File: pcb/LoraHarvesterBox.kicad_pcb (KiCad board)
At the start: 4 copper layers, 48 x 45.5 mm, 42 parts, among them J1 Conn_01x02_Pin, J2 Conn_01x02_Pin, J3 Conn_01x02_Pin, J4 Conn_01x04_Socket, J5 Conn_01x04_Socket, J6 Conn_01x04_Socket, J7 Conn_01x04_Socket, J8 Conn_01x06_Socket, SW1 SSSS811101, SW2 TS-1088-AR02016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

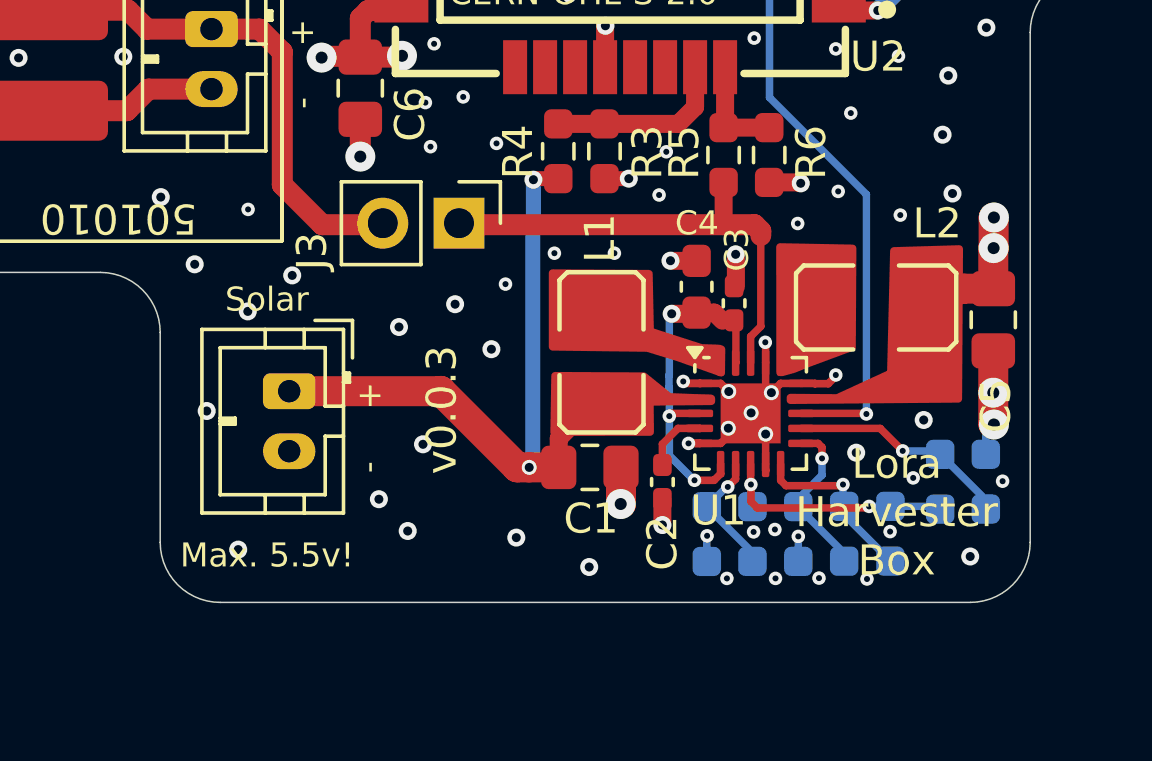
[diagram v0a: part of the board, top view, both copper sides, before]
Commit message: pcb: move silk screens and jumper around
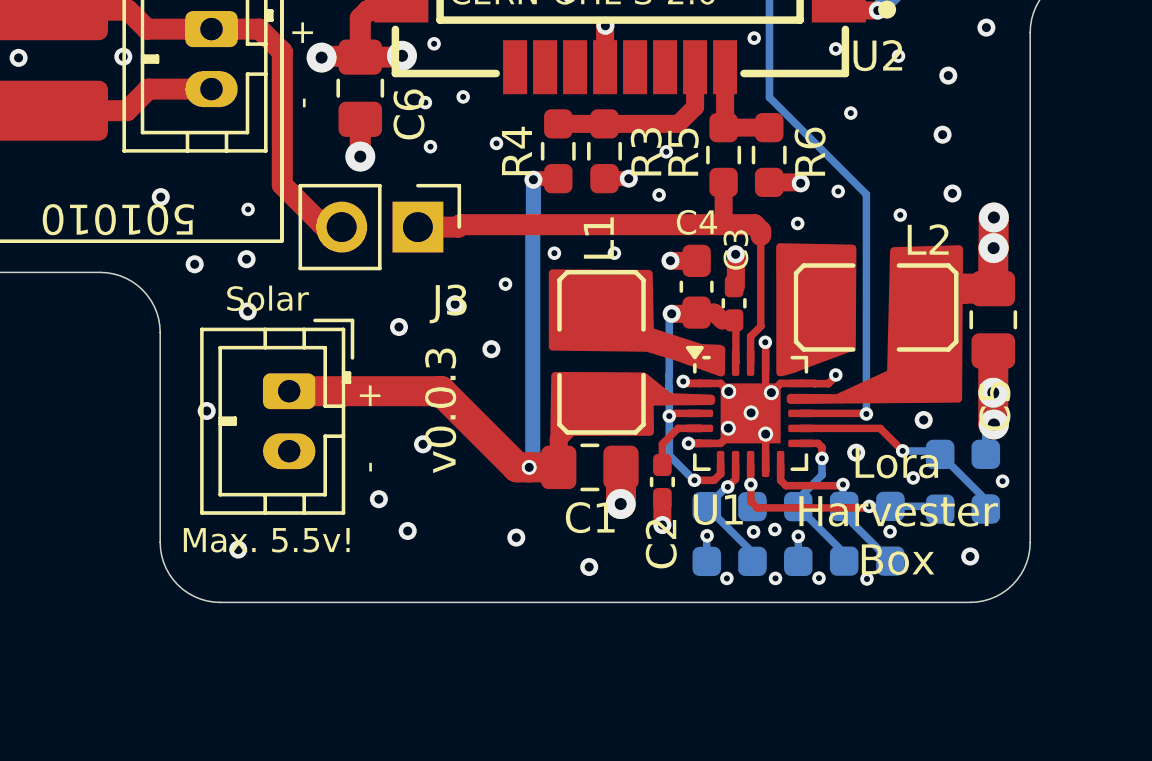
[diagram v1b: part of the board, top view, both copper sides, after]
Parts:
- moved J3 1.38 mm to (118.6, 87.5)
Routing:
- net /VBAT: track 16.1 -> 17.5 mm
- net Net-(BT1-+): track 17.7 -> 16.4 mm
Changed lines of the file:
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@@
 	(footprint "Connector_PinHeader_2.54mm:PinHeader_1x02_P2.54mm_Vertical"
 		(layer "F.Cu")
-		(at 119.96 87.36 -90)
+		(at 118.59 87.49 -90)
 		(descr "Through hole straight pin header, 1x02, 2.54mm pitch, single row")
 		(tags "Through hole pin header THT 1x02 2.54mm single row")
 		(property "Reference" "J3"
-			(at 0.93 4.9 90)
+			(at 2.47 -1.1 0)
 			(layer "F.SilkS")
 			(effects
@@
 		(at 133.86375 90.17)
 		(property "Reference" "L2"
-			(at 2.03625 -2.8 0)
+			(at 1.73625 -2.22 0)
 			(layer "F.SilkS")
 			(effects
@@
 	)
 	(gr_text "Max. 5.5v!"
-		(at 110.66 98.9 0)
+		(at 110.68 98.42 0)
 		(layer "F.SilkS")
 		(effects
@@
 	)
 	(segment
+		(start 128.76 87.41)
+		(end 120.01 87.41)
+		(width 0.7)
+		(layer "F.Cu")
+		(net 1)
+	)
+	(segment
 		(start 128.78 87.39)
 		(end 128.76 87.41)
@@
 	)
 	(segment
-		(start 128.76 87.41)
-		(end 120.01 87.41)
-		(width 0.7)
-		(layer "F.Cu")
-		(net 1)
-	)
-	(segment
 		(start 120.01 87.41)
-		(end 119.96 87.36)
+		(end 119.93 87.49)
 		(width 0.7)
 		(layer "F.Cu")
@@
 	)
 	(segment
+		(start 119.93 87.49)
+		(end 118.59 87.49)
+		(width 0.7)
+		(layer "F.Cu")
+		(net 1)
+	)
+	(segment
 		(start 129.81 87.41)
 		(end 128.76 87.41)
@@
 	)
 	(via
-		(at 114.4 89.1)
+		(at 112.88 88.56)
 		(size 0.6)
 		(drill 0.3)
@@
 	)
 	(segment
-		(start 113.31 80.89)
-		(end 111.71 80.89)
+		(start 115.97 87.41)
+		(end 115.4 87.41)
 		(width 0.7)
 		(layer "F.Cu")
@@
 	)
 	(segment
-		(start 109.56 80.89)
-		(end 111.71 80.89)
+		(start 116.05 87.49)
+		(end 115.97 87.41)
 		(width 0.7)
 		(layer "F.Cu")
@@
 	)
 	(segment
-		(start 114.07 81.65)
-		(end 113.31 80.89)
+		(start 115.4 87.41)
+		(end 114.07 86.08)
 		(width 0.7)
 		(layer "F.Cu")
@@
 	)
 	(segment
-		(start 117.42 87.36)
-		(end 117.37 87.41)
+		(start 109.56 80.89)
+		(end 111.71 80.89)
 		(width 0.7)
 		(layer "F.Cu")
@@
 	)
 	(segment
-		(start 108.93 80.26)
-		(end 109.56 80.89)
+		(start 114.07 86.08)
+		(end 114.07 81.65)
 		(width 0.7)
 		(layer "F.Cu")
@@
 	)
 	(segment
-		(start 115.4 87.41)
-		(end 114.07 86.08)
+		(start 108.93 80.26)
+		(end 109.56 80.89)
 		(width 0.7)
 		(layer "F.Cu")
@@
 	)
 	(segment
-		(start 117.37 87.41)
-		(end 115.4 87.41)
+		(start 114.07 81.65)
+		(end 113.31 80.89)
 		(width 0.7)
 		(layer "F.Cu")
@@
 	)
 	(segment
-		(start 114.07 86.08)
-		(end 114.07 81.65)
+		(start 113.31 80.89)
+		(end 111.71 80.89)
 		(width 0.7)
 		(layer "F.Cu")

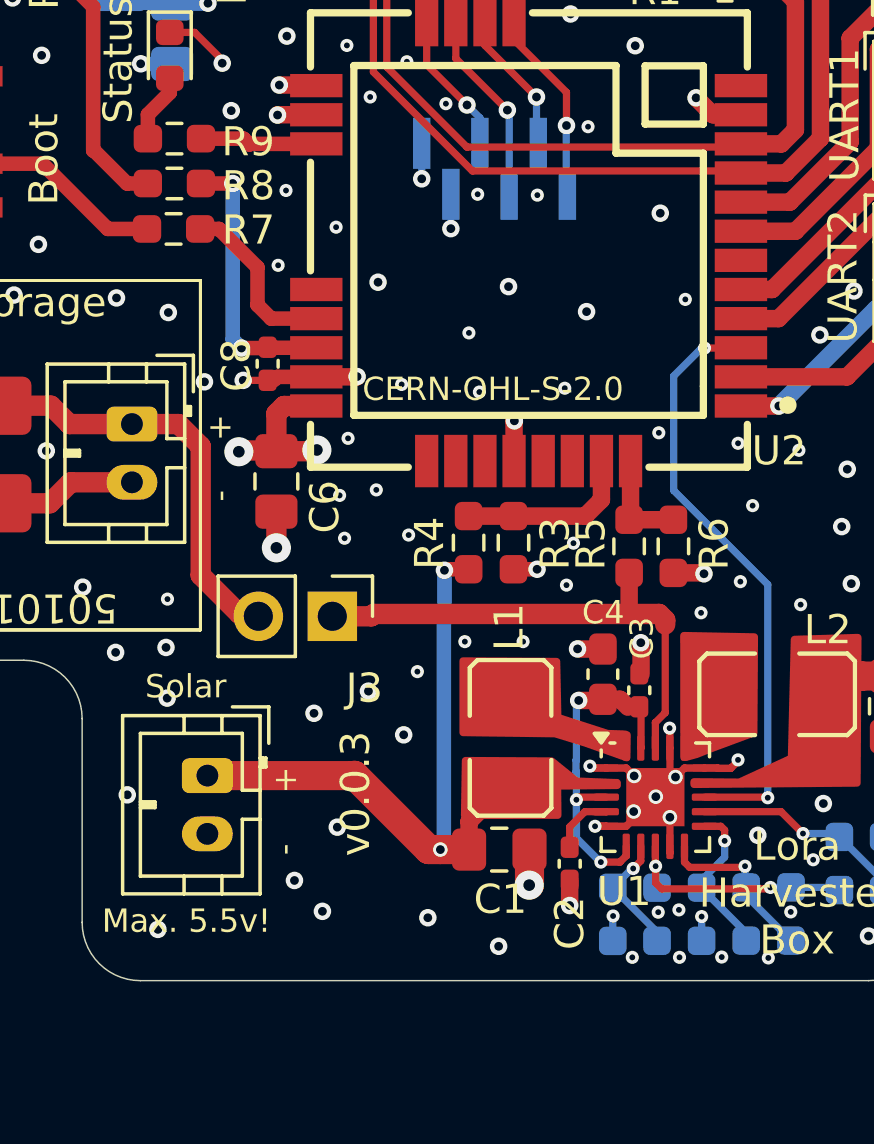
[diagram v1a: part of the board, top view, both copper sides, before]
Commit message: pcb, sch, doc: remove remaining 0401
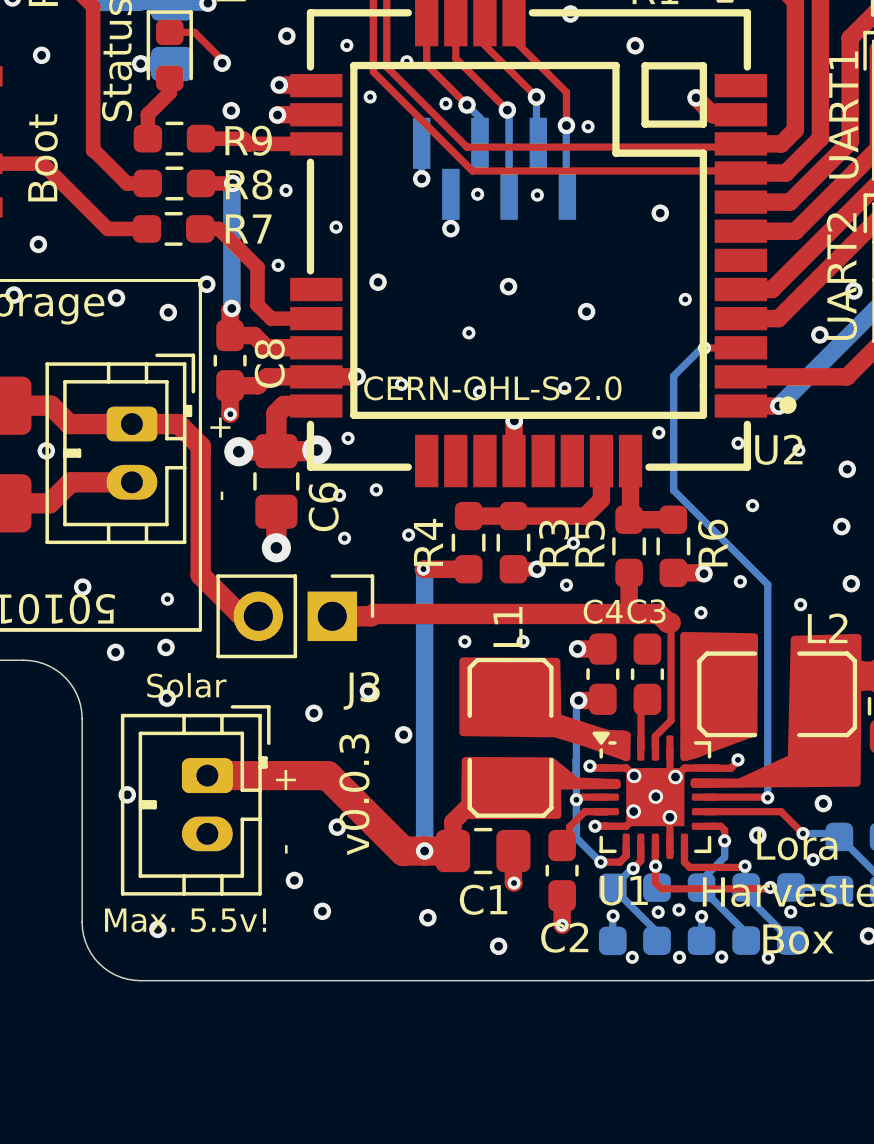
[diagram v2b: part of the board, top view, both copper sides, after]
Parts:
- C2, C3, C8: footprint Capacitor_SMD:C_0402_1005Metric_Pad0.74x0.62mm_HandSolder -> Capacitor_SMD:C_0603_1608Metric_Pad1.08x0.95mm_HandSolder
- moved C8 1.29 mm to (115.1, 78.7)
- moved C3 0.62 mm to (129.4, 89.5)
- moved C1 0.55 mm to (123.8, 95.5)
- moved C2 0.35 mm to (126.5, 96.2)
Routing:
- net /VSTOR: track 11.5 -> 10.5 mm
- net /VSOLAR: track 25.7 -> 26.5 mm
- net GND: vias 180 -> 177

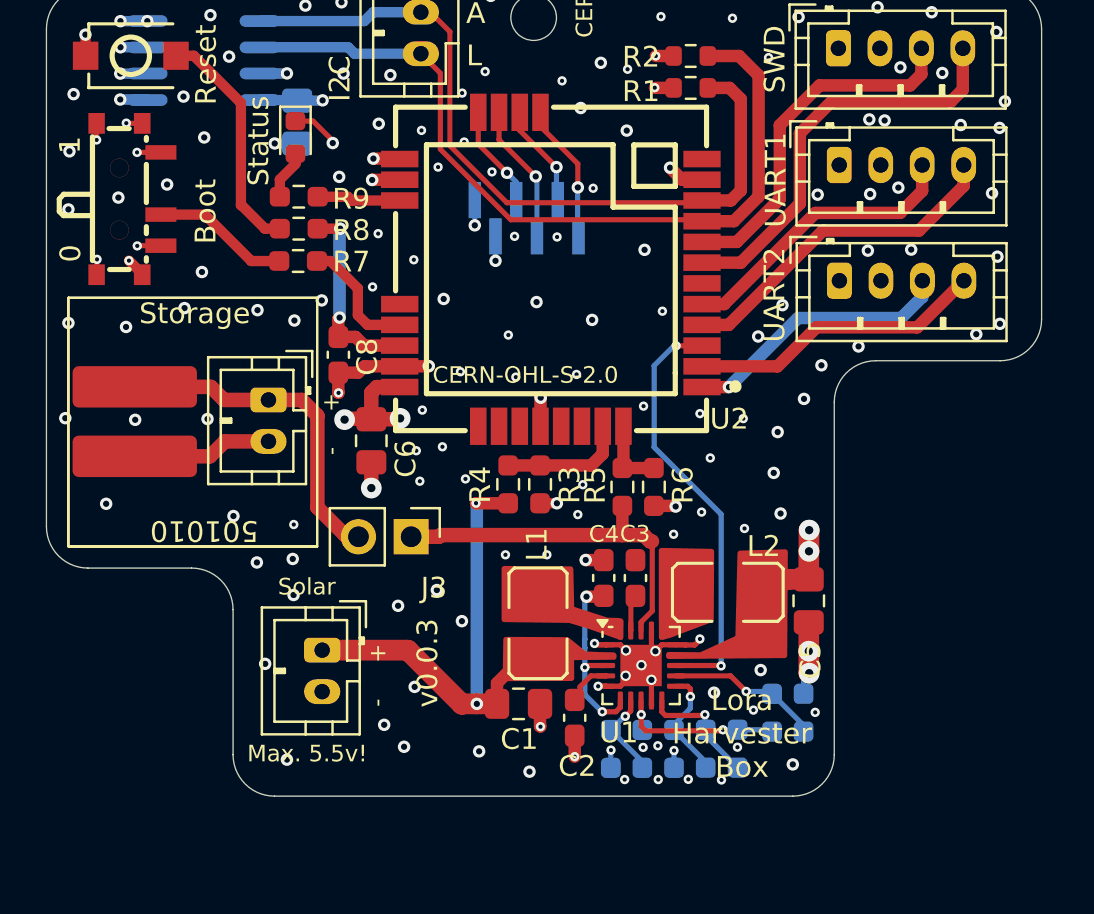
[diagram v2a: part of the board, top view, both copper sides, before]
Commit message: pcb, sch, doc: add buffer C for voltage dividers
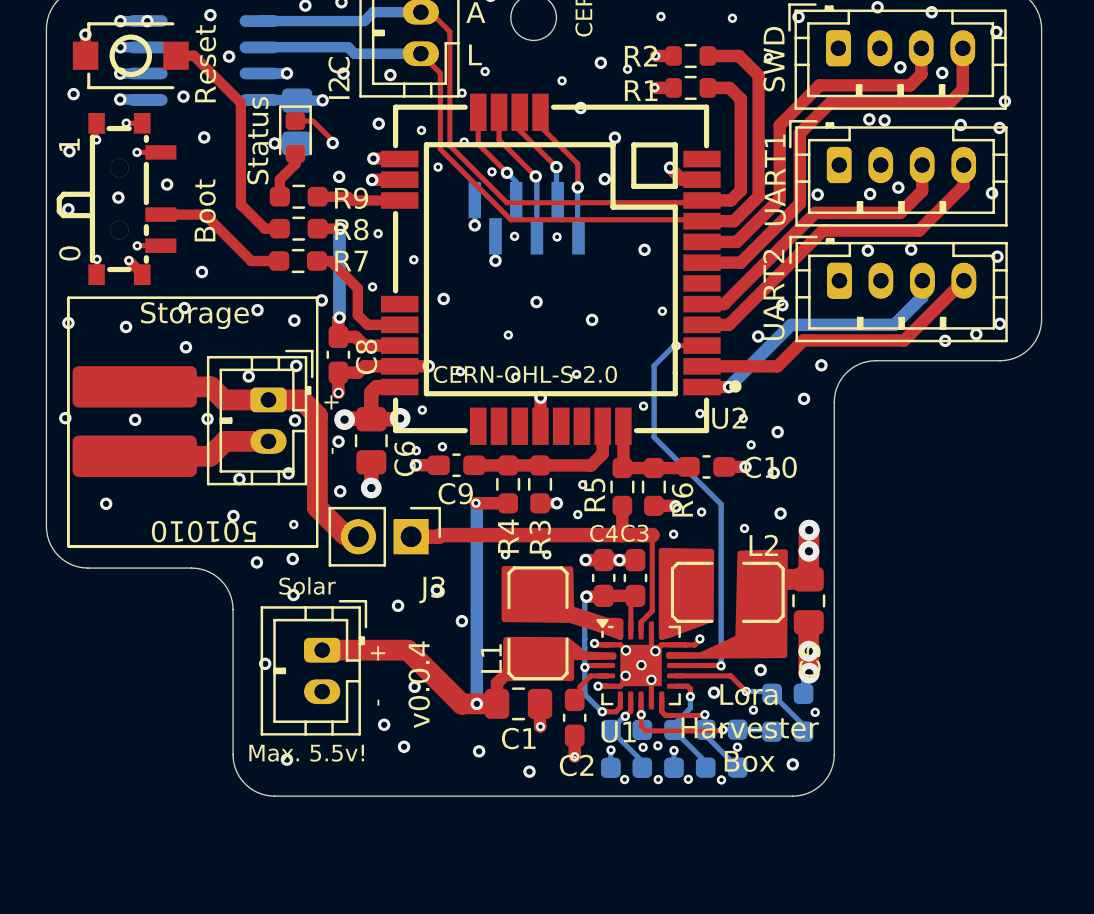
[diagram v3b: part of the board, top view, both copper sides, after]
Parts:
- added C10: 100nF, Capacitor_SMD:C_0603_1608Metric_Pad1.08x0.95mm_HandSolder, F.Cu at (132.8, 84.1)
- added C9: 100nf, Capacitor_SMD:C_0603_1608Metric_Pad1.08x0.95mm_HandSolder, F.Cu at (120.8, 84.0)
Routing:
- net GND: track 55.7 -> 59.4 mm, vias 177 -> 186
- net /ADC_BAT: track 3.56 -> 5.25 mm
- net /ADC_SOL: track 6.12 -> 7.75 mm
- net /VSTOR: track 10.5 -> 12.0 mm
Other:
- board text added: "v0.0.4"
- board text removed: "v0.0.3"
